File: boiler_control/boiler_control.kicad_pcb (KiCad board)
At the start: 2 copper layers, 115.1 x 59.9 mm, 55 parts, among them J1 Conn_01x01, J3V3 Conn_01x03, J5V1 Conn_01x03, U2 MOUDLE-SEEEDUINO-XIAO-ESP32C3, U4 MOC3162M

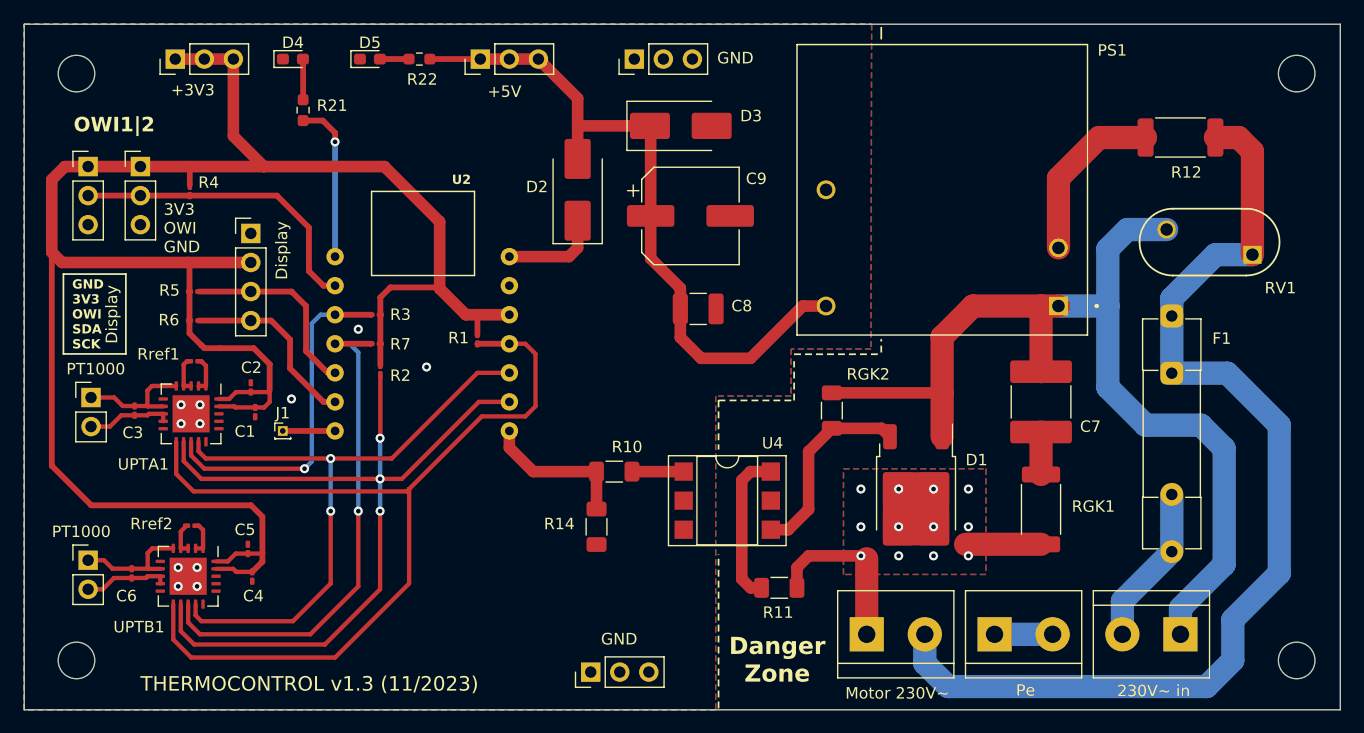
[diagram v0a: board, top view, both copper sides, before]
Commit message: Replace max3856 with SSOP package; replace all 0201 res/cap packages with 0603
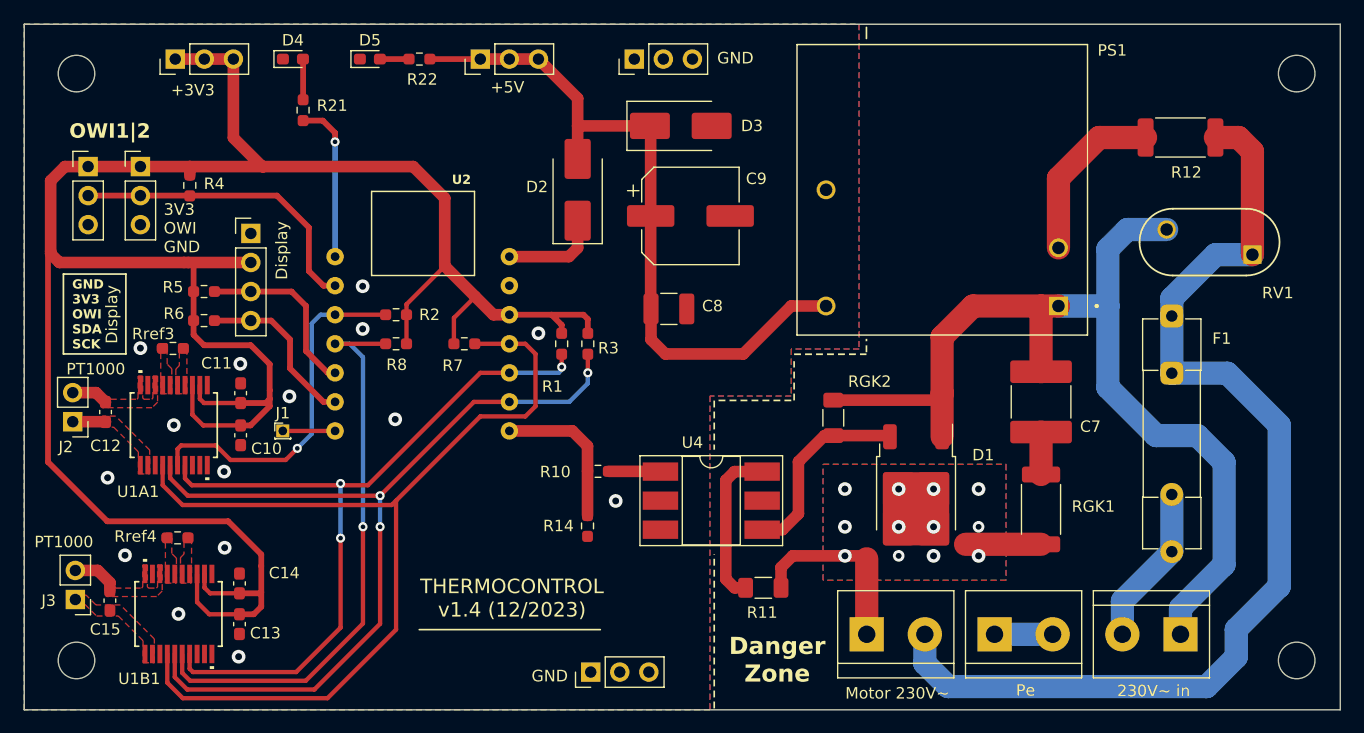
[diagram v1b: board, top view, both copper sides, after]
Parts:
- removed C1, C2, C4, C5: C, Capacitor_SMD:C_0201_0603Metric_Pad0.64x0.40mm_HandSolder
- removed C3, C6: 100nF, Capacitor_SMD:C_0201_0603Metric_Pad0.64x0.40mm_HandSolder
- removed JPTa1, JPTb1: Conn_01x02, Connector_PinHeader_2.54mm:PinHeader_1x02_P2.54mm_Vertical
- removed Rref1, Rref2: R, Resistor_SMD:R_0201_0603Metric_Pad0.64x0.40mm_HandSolder
- removed UPTA1, UPTB1: MAX31865xTP, Package_DFN_QFN:TQFN-20-1EP_5x5mm_P0.65mm_EP3.25x3.25mm
- added C10: 100n, Capacitor_SMD:C_0603_1608Metric_Pad1.08x0.95mm_HandSolder, F.Cu at (39.0, 56.0)
- added C11: 100n, Capacitor_SMD:C_0603_1608Metric_Pad1.08x0.95mm_HandSolder, F.Cu at (39.0, 52.3)
- added C12: 10nF, Capacitor_SMD:C_0603_1608Metric_Pad1.08x0.95mm_HandSolder, F.Cu at (27.2, 54.0)
- added C13: 100n, Capacitor_SMD:C_0603_1608Metric_Pad1.08x0.95mm_HandSolder, F.Cu at (38.9, 72.5)
- added C14: 100n, Capacitor_SMD:C_0603_1608Metric_Pad1.08x0.95mm_HandSolder, F.Cu at (38.9, 69.0)
- added C15: 10nF, Capacitor_SMD:C_0603_1608Metric_Pad1.08x0.95mm_HandSolder, F.Cu at (27.6, 70.5)
- added J2: Conn_01x02_Socket, Connector_PinHeader_2.54mm:PinHeader_1x02_P2.54mm_Vertical, F.Cu at (24.3, 54.8)
- added J3: Conn_01x02_Socket, Connector_PinHeader_2.54mm:PinHeader_1x02_P2.54mm_Vertical, F.Cu at (24.5, 70.4)
- added R8: 1k, Resistor_SMD:R_0603_1608Metric_Pad0.98x0.95mm_HandSolder, F.Cu at (52.6, 48.0)
- added Rref3: R, Resistor_SMD:R_0603_1608Metric_Pad0.98x0.95mm_HandSolder, F.Cu at (33.1, 48.4)
- added Rref4: R, Resistor_SMD:R_0603_1608Metric_Pad0.98x0.95mm_HandSolder, F.Cu at (33.5, 65.0)
- added U1A1: MAX31865AAP+T, MAX31865AAP_T:21-0056C_20_MXM, F.Cu at (33.1, 55.1)
- added U1B1: MAX31865AAP+T, MAX31865AAP_T:21-0056C_20_MXM, F.Cu at (33.6, 71.6)
- R1, R2, R3, R4, R5, R6, R7: footprint Resistor_SMD:R_0201_0603Metric_Pad0.64x0.40mm_HandSolder -> Resistor_SMD:R_0603_1608Metric_Pad0.98x0.95mm_HandSolder
- R10, R14: footprint Resistor_SMD:R_1206_3216Metric_Pad1.30x1.75mm_HandSolder -> Resistor_SMD:R_0603_1608Metric_Pad0.98x0.95mm_HandSolder
- RGK1: value 39 -> 39 1/2W
- U4: footprint Package_DIP:DIP-6_W7.62mm_SMDSocket_SmallPads -> Package_DIP:DIP-6_W8.89mm_SMDSocket_LongPads
- moved R3 18.7 mm to (69.3, 48.0), turned to -90 degrees
- moved R7 7.75 mm to (58.5, 48.0), turned to 0 degrees
- moved R1 7.38 mm to (67.1, 48.0)
- moved R2 5.03 mm to (52.6, 45.5), turned to 180 degrees
- moved C8 2.57 mm to (76.4, 45.0)
- moved R10 1.42 mm to (70.2, 59.2)
- moved U4 1.40 mm to (80.1, 61.7)
- moved R11 1.40 mm to (84.7, 69.3)
- moved R5 0.86 mm to (35.8, 43.4)
- moved R6 0.86 mm to (35.8, 46.0)
- moved R14 0.79 mm to (69.3, 63.9)
- moved RGK2 0.65 mm to (90.8, 54.5)
- moved R4 0.48 mm to (34.5, 34.2)
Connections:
- R1 pad 2: spi_sdi -> spi_sdo
- R2 pad 2: spi_sck -> spi_cs1
- R3 pad 2: spi_cs1 -> spi_sck
- R7 pad 2: spi_cs2 -> spi_sdi
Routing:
- net +3V3: track 182.7 -> 210.3 mm
- net spi_sdo: track 56.7 -> 68.7 mm, vias 2 -> 3
- net Net-(JPTa1-Pin_1): track 10.7 -> 0.00 mm
- net Net-(JPTb1-Pin_1): track 10.4 -> 0.00 mm
- net Net-(JPTb1-Pin_2): track 7.43 -> 0.00 mm
- net Net-(JPTa1-Pin_2): track 7.42 -> 0.00 mm
- net spi_cs2: track 44.6 -> 50.4 mm
- net spi_sck: track 74.6 -> 78.9 mm
- net Net-(J3-Pin_2): track 0.00 -> 4.17 mm
- net Net-(J2-Pin_2): track 0.00 -> 3.22 mm
- net Net-(UPTA1-BIAS): track 3.20 -> 0.00 mm
- net Net-(UPTA1-ISENSOR): track 3.15 -> 0.00 mm
- net Net-(UPTB1-BIAS): track 3.04 -> 0.00 mm
- net Net-(J2-Pin_1): track 0.00 -> 2.88 mm
- net Net-(UPTB1-ISENSOR): track 2.84 -> 0.00 mm
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- added copper zone on F.Cu, net Net-(J2-Pin_1)
- added copper zone on F.Cu, net Net-(J2-Pin_2)
- added copper zone on F.Cu, net Net-(J3-Pin_1)
- added copper zone on F.Cu, net Net-(J3-Pin_2)
- added copper zone on F.Cu, net Net-(U1A1-BIAS)
- added copper zone on F.Cu, net Net-(U1A1-ISENSOR)
- added copper zone on F.Cu, net Net-(U1B1-BIAS)
- added copper zone on F.Cu, net Net-(U1B1-ISENSOR)
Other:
- board text added: "THERMOCONTROL v1.4 (12/2023)"
- board text removed: "THERMOCONTROL v1.3 (11/2023)"

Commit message: Updating to v1.4 - pushed to order
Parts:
- removed Rref3, Rref4: R, Resistor_SMD:R_0603_1608Metric_Pad0.98x0.95mm_HandSolder
- added Rref1: 4.3k 0.1%, Resistor_SMD:R_0603_1608Metric_Pad0.98x0.95mm_HandSolder, F.Cu at (33.0, 48.4)
- added Rref2: 4.3k 0.1%, Resistor_SMD:R_0603_1608Metric_Pad0.98x0.95mm_HandSolder, F.Cu at (33.5, 64.9)
- F1: footprint Fuse:Fuseholder_Clip-5x20mm_Schurter_CQM_Inline_P20.60x5.00mm_D1.00mm_Horizontal -> Fuse:Fuseholder_Clip-5x20mm_Littelfuse_445-030_Inline_P20.50x5.20mm_D1.30mm_Horizontal
- J1: footprint Connector_PinHeader_1.00mm:PinHeader_1x01_P1.00mm_Vertical -> Connector_PinHeader_2.54mm:PinHeader_1x01_P2.54mm_Vertical
- R10: value Rift -> 270
- R21: value R -> 100
- R22: value R -> 330
- moved J_230V_in1 5.08 mm to (116.1, 73.4), turned to 0 degrees
- moved F1 4.45 mm to (124.8, 46.2)
- moved RV1 3.39 mm to (120.4, 38.4), turned to -90 degrees
- moved R12 3.27 mm to (121.5, 26.7), turned to 90 degrees
- moved C7 1.52 mm to (110.5, 53.1)
- moved RGK1 1.52 mm to (110.5, 62.5)
- moved H3 1.49 mm to (130.0, 75.0)
- moved H2 1.37 mm to (130.0, 24.0)
- moved H1 0.74 mm to (24.0, 24.0)
- moved H4 0.71 mm to (24.0, 76.0)
- moved J1 0.13 mm to (42.5, 55.6)
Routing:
- net Net-(PS1-AC(L)): track 15.2 -> 24.9 mm
- net power_230V_N: track 87.3 -> 77.9 mm
- net power_230V_L1_fused: track 92.7 -> 84.6 mm
- net /motor_control/triac_com: track 23.0 -> 21.7 mm, vias 12 -> 18
- net +5V: track 62.1 -> 63.3 mm
- net Net-(D1-G): track 17.3 -> 18.0 mm
- net power_230V_L1: track 14.0 -> 13.5 mm
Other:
- board size 115.1 x 59.9 mm -> 114 x 60 mm
- board text added: "230V~"

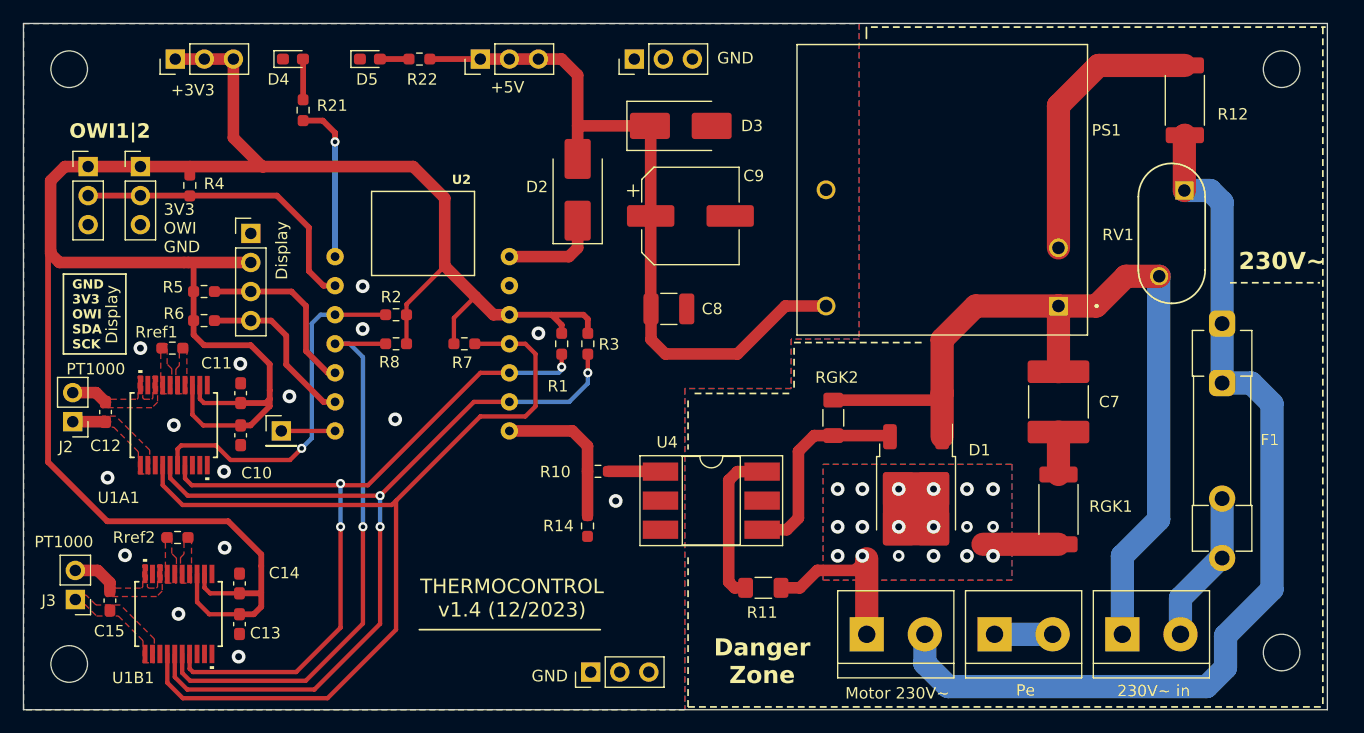
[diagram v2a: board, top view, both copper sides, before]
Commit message: Adding JB1 jumper for bridge change size of connectors for pt1000 to 3.5 mm some cosmetics
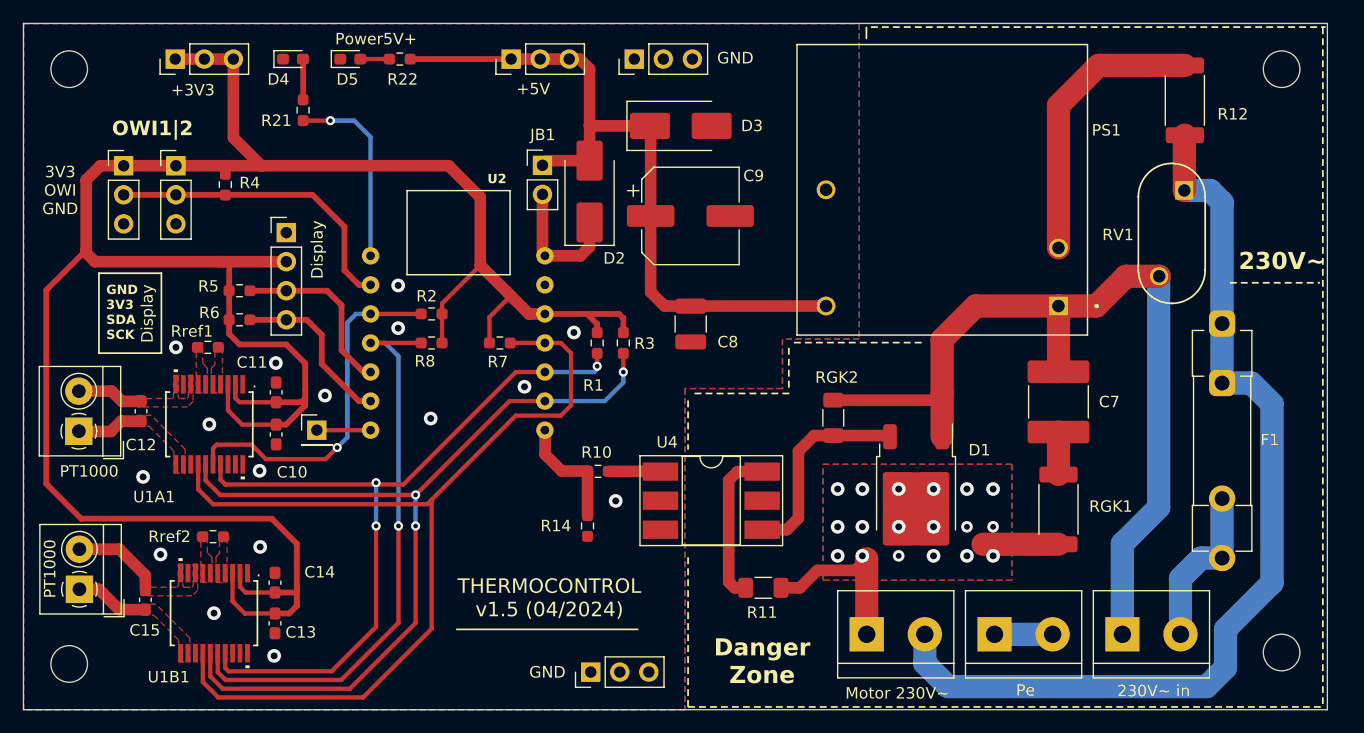
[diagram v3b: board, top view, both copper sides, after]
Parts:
- added JB1: Conn_01x02_Pin, Connector_PinHeader_2.54mm:PinHeader_1x02_P2.54mm_Vertical, F.Cu at (65.4, 32.4)
- J2, J3: footprint Connector_PinHeader_2.54mm:PinHeader_1x02_P2.54mm_Vertical -> TerminalBlock_4Ucon:TerminalBlock_4Ucon_1x02_P3.50mm_Horizontal
- moved R1 3.11 mm to (70.2, 47.9)
- moved C10 3.11 mm to (42.1, 55.9)
- moved C11 3.11 mm to (42.1, 52.3)
- moved C13 3.11 mm to (42.0, 72.4)
- moved C14 3.11 mm to (42.0, 68.9)
- moved JDisplay1 3.11 mm to (43.0, 38.3)
- moved JOWI1 3.11 mm to (28.8, 32.4)
- moved JOWI2 3.11 mm to (33.3, 32.4)
- moved R4 3.11 mm to (37.6, 34.1)
- moved R7 3.11 mm to (61.7, 47.9)
- moved Rref2 3.11 mm to (36.6, 64.9)
- moved U1A1 3.11 mm to (36.3, 55.0)
- moved U1B1 3.11 mm to (36.7, 71.6)
- moved U2 3.11 mm to (50.3, 58.1)
- moved C12 3.11 mm to (30.3, 53.9)
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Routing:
- net Net-(J3-Pin_1): track 0.00 -> 6.51 mm
- net +3V3: track 210.3 -> 216.1 mm
- net Net-(J3-Pin_2): track 4.17 -> 7.99 mm
- net Net-(D2-K): track 8.66 -> 11.8 mm
- net motor_ctrl: track 13.4 -> 10.3 mm
- net Net-(J2-Pin_1): track 2.88 -> 5.83 mm
- net led: track 14.1 -> 16.9 mm
- net Net-(J2-Pin_2): track 3.22 -> 5.81 mm
- net power_230V_L1: track 13.5 -> 14.5 mm
- net +5V: track 63.3 -> 64.0 mm
- net GND: vias 15 -> 16
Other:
- board text added: "."
- board text added: "GND 3V3 SDA SCK"
- board text added: "Power5V+"
- board text added: "THERMOCONTROL v1.5 (04/2024)"
- board text removed: "GND 3V3 OWI SDA SCK"
- board text removed: "THERMOCONTROL v1.4 (12/2023)"

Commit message: All cosmetics
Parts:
- moved JGND2 2.44 mm to (67.2, 76.7)
- moved R4 1.40 mm to (37.6, 32.7)
- moved JOWI1 1.40 mm to (28.7, 31.0)
- moved JOWI2 1.40 mm to (33.3, 31.0)
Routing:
- net owi: track 27.1 -> 28.7 mm
- net power_230V_L1_fused: track 84.6 -> 83.1 mm
- net +3V3: track 216.1 -> 216.7 mm
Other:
- board text added: "ESP32"
